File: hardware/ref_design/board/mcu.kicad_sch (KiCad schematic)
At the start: 10 parts, among them U4 RP2350B, U5 W25Q128JVPIQ, X1 12MHz

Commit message: Reference design: board routed and DRC clean
- Core copy made faithful: Raspberry Pi's 0402 land patterns for the core
  passives (tools/lib_from_ref.py), their 3V3 stubs into the pour under the
  chip kept, and the uncopied-pad check made layer-aware (their board has a
  second flash footprint on the back, which had cost every QSPI track).
- TPS63001 re-placed and its power loop drawn by route.py as TI's layout
  guidance asks.
- tools/maze.py: a small A* router for the flash's SD2 line and for any
  connection Freerouting leaves open, with bounded rip-up.
- route.py: order-stable pre-routes (so --reuse is valid), fiducial
  keep-outs for the router, a second Freerouting pass when needed with a
  watchdog for its warning dialog, loose-copper cleanup.

check_pcb.py: 0 errors, 0 unconnected, 0 schematic parity issues.

Co-Authored-By: Claude Opus 5.5 (1M context) <noreply@anthropic.com>
Claude-Session: https://claude.ai/code/session_01KGgEu3CbFtCsvHRQgAFiCN
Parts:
- C27, C28: footprint Capacitor_SMD:C_0402_1005Metric -> battler:C_0402_1005Metric_RPi
- R20, R21, R22, R23, R24: footprint Resistor_SMD:R_0402_1005Metric -> battler:R_0402_1005Metric_RPi
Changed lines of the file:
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@@
         (font
           (size 1.27 1.27))))
-    (property "Footprint" "Capacitor_SMD:C_0402_1005Metric"
+    (property "Footprint" "battler:C_0402_1005Metric_RPi"
       (at 203.2 35.56 0)
       (effects
@@
         (font
           (size 1.27 1.27))))
-    (property "Footprint" "Capacitor_SMD:C_0402_1005Metric"
+    (property "Footprint" "battler:C_0402_1005Metric_RPi"
       (at 228.6 35.56 0)
       (effects
@@
         (font
           (size 1.27 1.27))))
-    (property "Footprint" "Resistor_SMD:R_0402_1005Metric"
+    (property "Footprint" "battler:R_0402_1005Metric_RPi"
       (at 175.26 35.56 0)
       (effects
@@
         (font
           (size 1.27 1.27))))
-    (property "Footprint" "Resistor_SMD:R_0402_1005Metric"
+    (property "Footprint" "battler:R_0402_1005Metric_RPi"
       (at 182.88 50.8 0)
       (effects
@@
         (font
           (size 1.27 1.27))))
-    (property "Footprint" "Resistor_SMD:R_0402_1005Metric"
+    (property "Footprint" "battler:R_0402_1005Metric_RPi"
       (at 226.06 50.8 0)
       (effects
@@
         (font
           (size 1.27 1.27))))
-    (property "Footprint" "Resistor_SMD:R_0402_1005Metric"
+    (property "Footprint" "battler:R_0402_1005Metric_RPi"
       (at 193.04 63.5 0)
       (effects
@@
         (font
           (size 1.27 1.27))))
-    (property "Footprint" "Resistor_SMD:R_0402_1005Metric"
+    (property "Footprint" "battler:R_0402_1005Metric_RPi"
       (at 226.06 63.5 0)
       (effects

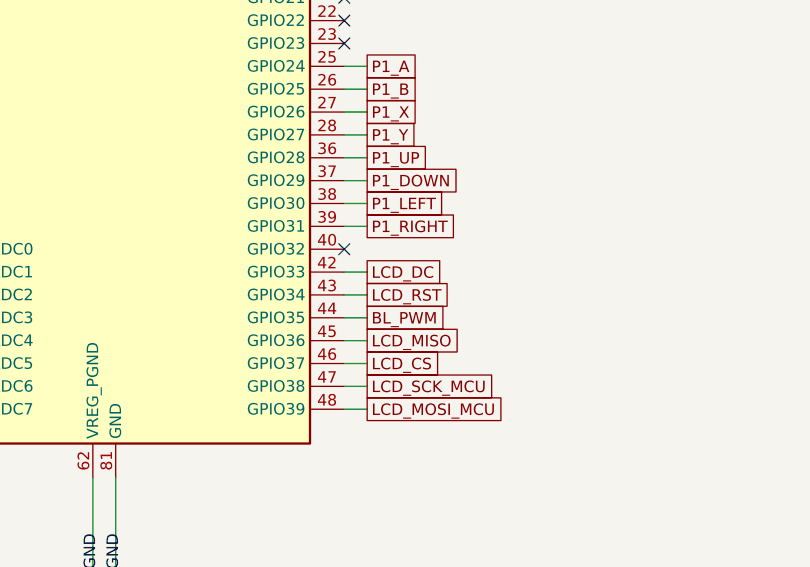
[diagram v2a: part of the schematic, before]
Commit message: Reference design: QD3525 panel, fab outputs, fit check
The $25-35 Displaytech DT035 is replaced by the QD3525, a bare 3.5in IPS
ST7796U panel of the same class at about $5-8 with a published drawing
and pinout (the panel inside LCDwiki's MSP3525 module).

- J3 is now the landing for its 48-contact solder tail (tools/fp_panel.py),
  wired as the maker's module wires it; TE goes to GPIO32.
- Backlight: an AP3156 charge pump drives each of the six parallel LEDs
  through its own current sink, set over one GPIO (BL_SDI). Its symbol
  comes from tools/sym_lib.py (Konnect's create_symbol draws no body).
- case.scad is built around a fixed panel bay, so the board outline,
  buttons and screws stay put; the lid, lens and STLs follow the panel.
- Routing: fan-out vias kept off pads, the AP3156's GND pins stubbed into
  its thermal pad, loose copper trimmed at the end; silk.py re-runnable.
- fab/: gerbers and drill, JLC BOM (40 part numbers) and CPL (91
  placements), STEP, renders, schematic and assembly PDFs.

check_netlist: PASS. ERC: 0 errors. DRC: 0 errors, 0 unconnected,
0 parity issues (2 cosmetic silk warnings at the USB-C). check_fit: PASS.

Co-Authored-By: Claude Opus 5.5 (1M context) <noreply@anthropic.com>
Claude-Session: https://claude.ai/code/session_01KGgEu3CbFtCsvHRQgAFiCN
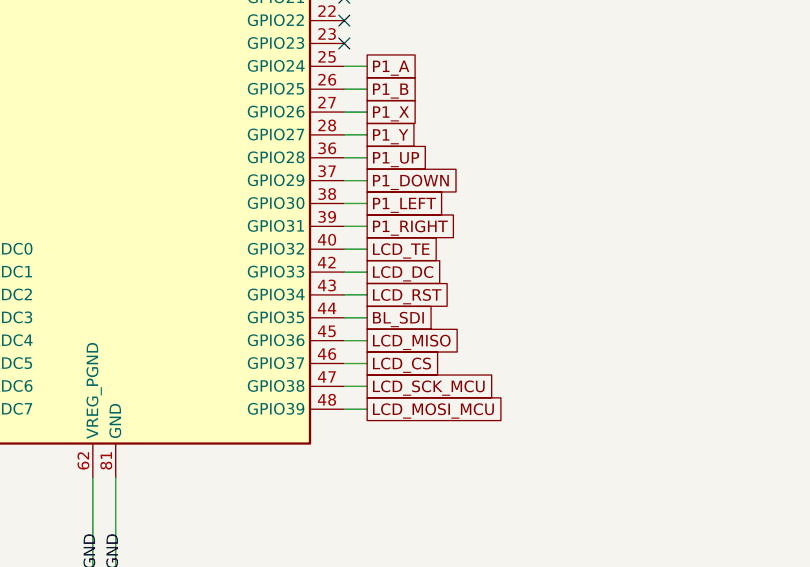
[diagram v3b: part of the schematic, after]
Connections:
- net LCD_TE: now reaches U4.40 (GPIO32)
- net BL_PWM renamed BL_SDI
- no-connect marks 9 -> 8
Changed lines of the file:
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@@
-)
-  (no_connect
-    (at 99.06 127)
 )
   (no_connect
@@
       (xy 99.06 124.46)
       (xy 101.6 124.46))
+)
+  (wire
+    (pts
+      (xy 99.06 127)
+      (xy 101.6 127))
 )
   (wire
@@
     (at 101.6 124.46 0)
 )
+  (global_label "LCD_TE"
+    (shape passive)
+    (at 101.6 127 0)
+)
   (global_label "LCD_DC"
     (shape passive)
@@
     (at 101.6 132.08 0)
 )
-  (global_label "BL_PWM"
+  (global_label "BL_SDI"
     (shape passive)
     (at 101.6 134.62 0)

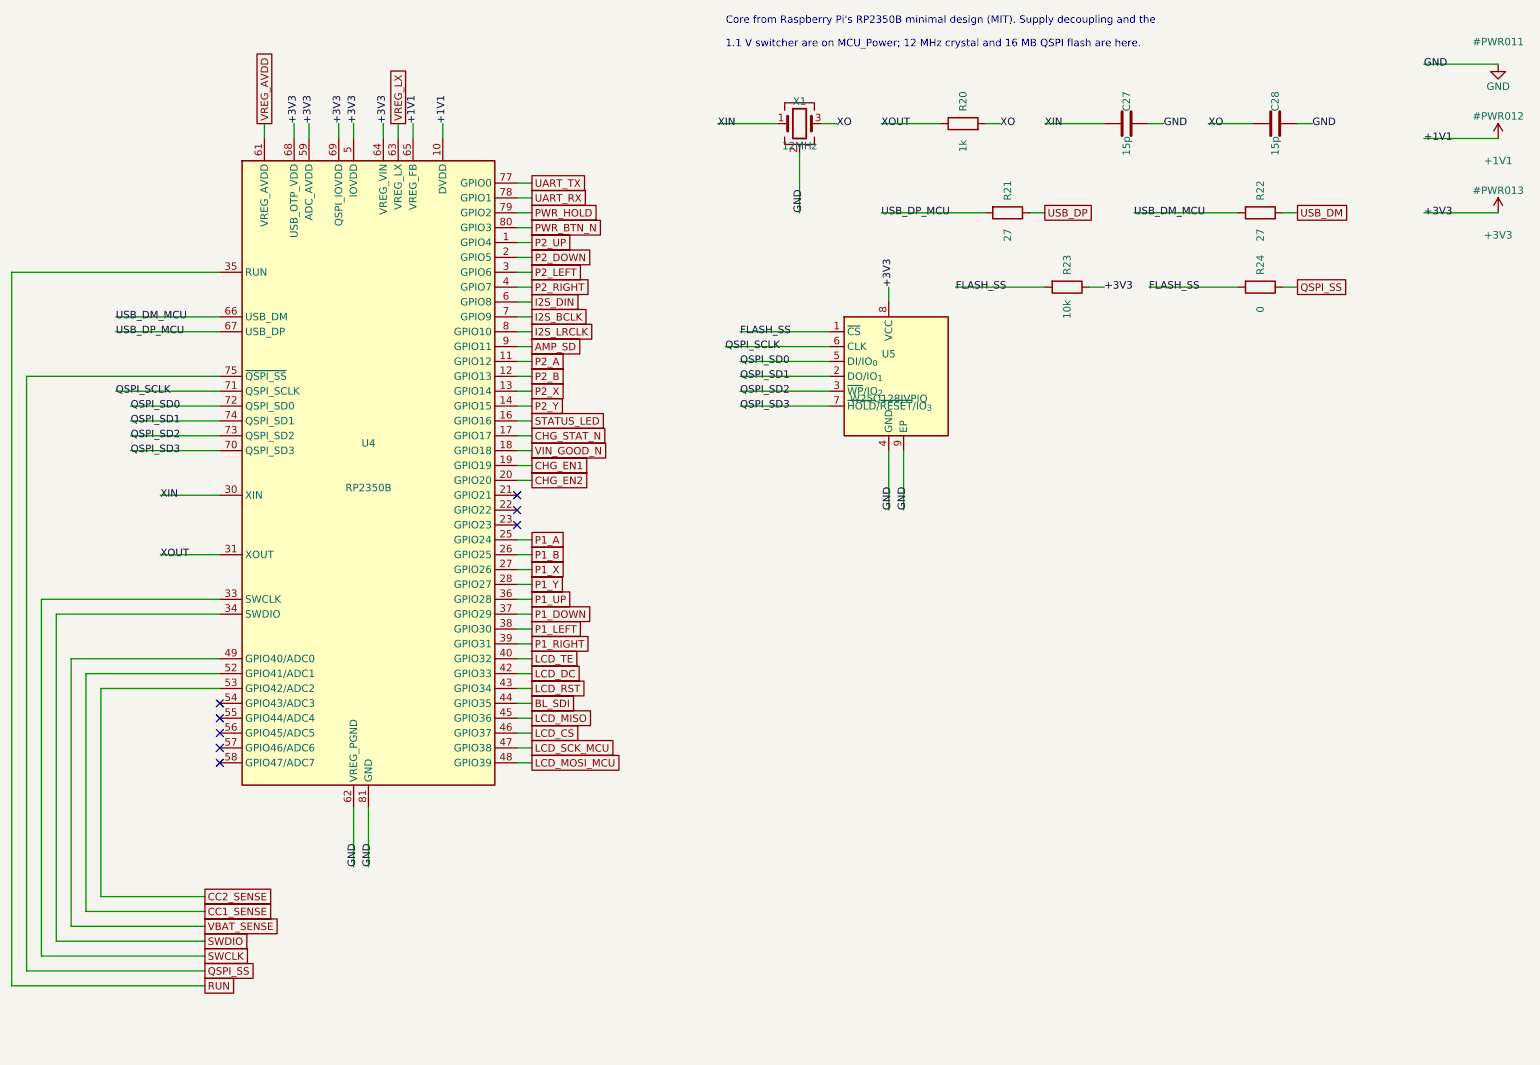
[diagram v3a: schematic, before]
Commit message: 2-layer fork: approved circuit changes in the design data and schematic
TP4056 charger (500 mA, TEMP grounded) with USB load sharing (B5819W, AO3401A
gate fed through a BAT54WS so it switches at once on an unplug, 22 uF on VSYS),
ME6211 3V3 LDO on the power latch, RP2354B with its flash inside (only the
QSPI_SS strap outside), 27 ohm 0603 USB resistors, SRV05-4 ESD, PWM audio
through two RC poles into an FM8002A, seat 1's Y contact as the power button,
no LEDs, no thermistor. Thermal-via footprints use 0.3 mm holes. Netlist
check passes, ERC 0 errors.

Co-Authored-By: Claude Opus 5.5 <noreply@anthropic.com>
Claude-Session: https://claude.ai/code/session_01KGgEu3CbFtCsvHRQgAFiCN
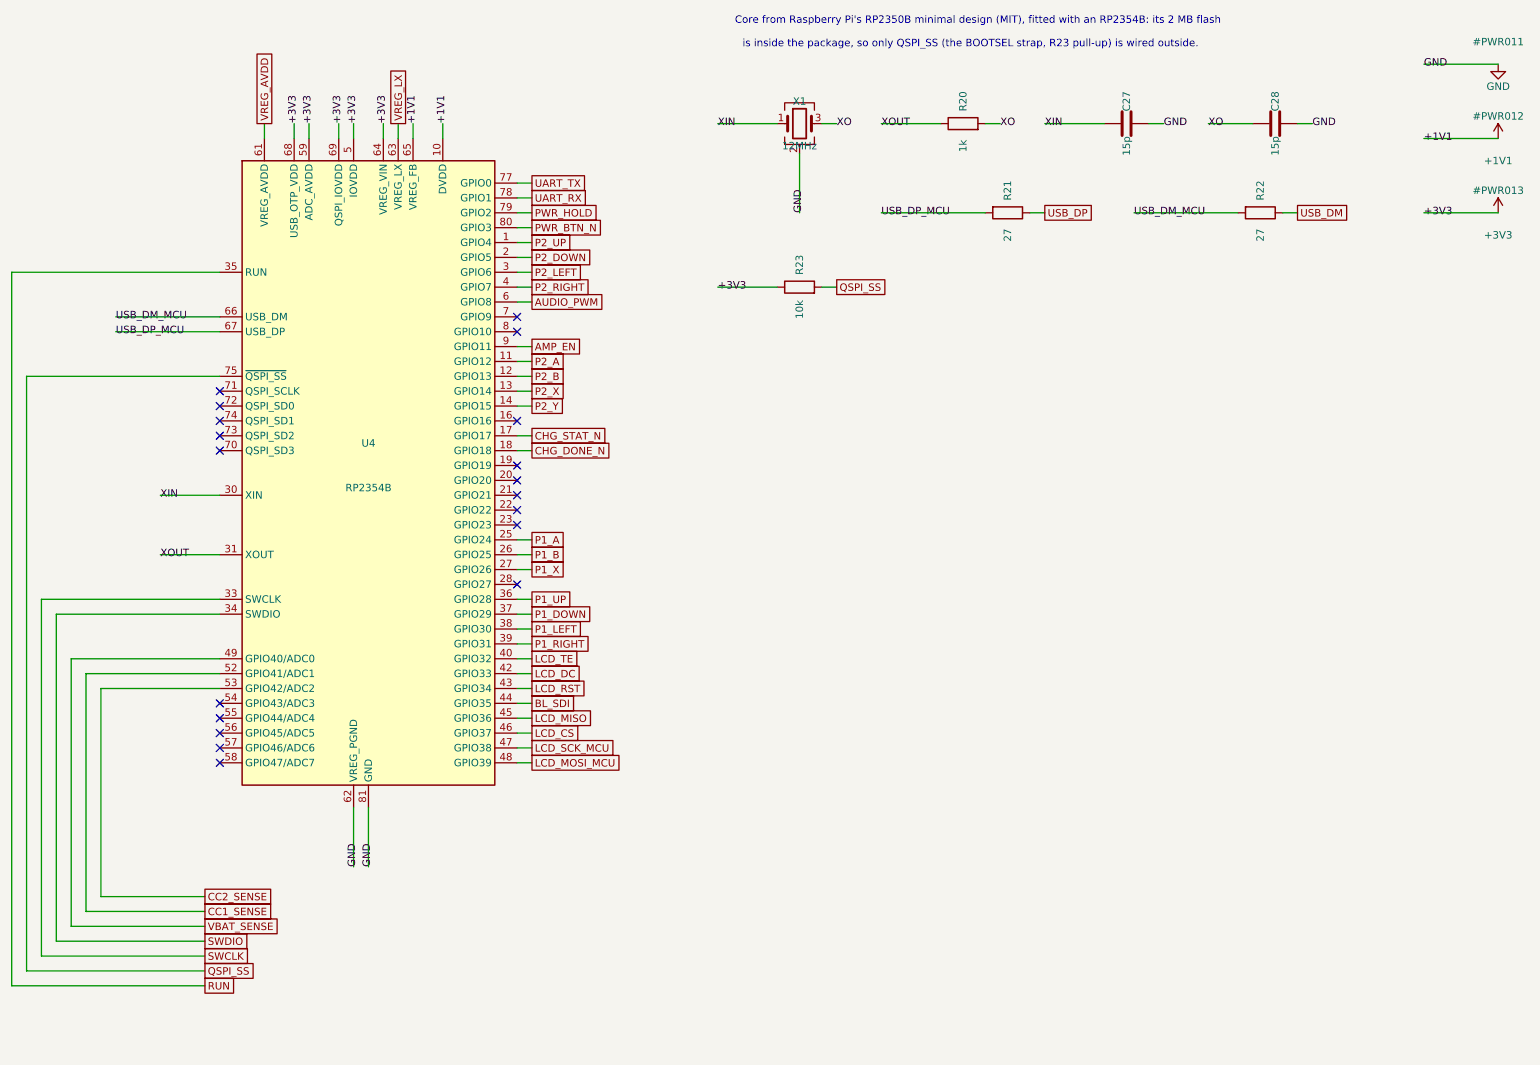
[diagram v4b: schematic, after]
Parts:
- removed R24: 0, battler:R_0402_1005Metric_RPi, symbol Device:R
- removed U5: W25Q128JVPIQ, Package_SON:WSON-8-1EP_6x5mm_P1.27mm_EP3.4x4.3mm, symbol Memory_Flash:W25Q32JVZP
- R21, R22: footprint battler:R_0402_1005Metric_RPi -> Resistor_SMD:R_0603_1608Metric; LCSC C25100 -> C25190; MPN 0402WGF270JTCE -> 0603WAF270JT5E
- U4: value RP2350B -> RP2354B; LCSC C42415655 -> C39843328; MPN RP2350B -> RP2354B
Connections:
- net FLASH_SS is gone; now on net QSPI_SS: R23.2
- net AMP_SD renamed AMP_EN
- net CHG_EN1: no longer names the net of U4.19 (GPIO19)
- net CHG_EN2: no longer names the net of U4.20 (GPIO20)
- net I2S_BCLK: no longer names the net of U4.7 (GPIO9)
- net I2S_DIN renamed AUDIO_PWM
- net I2S_LRCLK: no longer names the net of U4.8 (GPIO10)
- net P1_Y: no longer names the net of U4.28 (GPIO27)
- net QSPI_SCLK: no longer names the net of U4.71 (QSPI_SCLK)
- net QSPI_SD0: no longer names the net of U4.72 (QSPI_SD0)
- net QSPI_SD1: no longer names the net of U4.74 (QSPI_SD1)
- net QSPI_SD2: no longer names the net of U4.73 (QSPI_SD2)
- net QSPI_SD3: no longer names the net of U4.70 (QSPI_SD3)
- net STATUS_LED: no longer names the net of U4.16 (GPIO16)
- net VIN_GOOD_N renamed CHG_DONE_N
- no-connect marks 8 -> 19
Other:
- note added: "Core from Raspberry Pi's RP2350B minimal design (MIT), fitted with an RP2354B: its 2 MB flash"
- note added: "is inside the package, so only QSPI_SS (the BOOTSEL strap, R23 pull-up) is wired outside."
- note removed: "1.1 V switcher are on MCU_Power; 12 MHz crystal and 16 MB QSPI flash are here."
- note removed: "Core from Raspberry Pi's RP2350B minimal design (MIT). Supply decoupling and the"
